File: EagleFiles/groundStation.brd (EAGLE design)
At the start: 100 x 80 mm, 5 parts

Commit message: small changes in motor control
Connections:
- removed net N$13: U$2.GND
- removed net N$14: U$2.FLT_N
- removed net N$26: U$4.FLT_N
- net GND: now also U$2.GND
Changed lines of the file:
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@@
 <contactref element="U$1" pad="GND@0"/>
 <contactref element="U$1" pad="GND@1"/>
+<contactref element="U$2" pad="GND"/>
 <wire x1="-25.4" y1="-38.1" x2="-25.4" y2="-48.26" width="0" layer="19" extent="1-1"/>
 <wire x1="-2.54" y1="-48.26" x2="-25.4" y2="-48.26" width="0" layer="19" extent="1-1"/>
@@
 <wire x1="15.24" y1="-46.99" x2="-2.54" y2="-48.26" width="0" layer="19" extent="1-1"/>
 <wire x1="15.24" y1="-31.75" x2="15.24" y2="-46.99" width="0" layer="19" extent="1-1"/>
-<wire x1="15.24" y1="-6.35" x2="15.24" y2="-31.75" width="0" layer="19" extent="1-1"/>
+<wire x1="15.24" y1="-21.59" x2="15.24" y2="-31.75" width="0" layer="19" extent="1-1"/>
+<wire x1="15.24" y1="-6.35" x2="15.24" y2="-21.59" width="0" layer="19" extent="1-1"/>
 </signal>
 <signal name="N$5">
@@
 <wire x1="26.67" y1="-30.48" x2="15.24" y2="-41.91" width="0" layer="19" extent="1-1"/>
 </signal>
-<signal name="N$13">
-<contactref element="U$2" pad="GND"/>
-</signal>
-<signal name="N$14">
-<contactref element="U$2" pad="FLT_N"/>
-</signal>
 <signal name="V_EXTERNAL">
 <contactref element="U$2" pad="VMOT"/>
@@
 <wire x1="15.24" y1="-29.21" x2="15.24" y2="-3.81" width="0" layer="19" extent="1-1"/>
 </signal>
-<signal name="N$26">
-<contactref element="U$4" pad="FLT_N"/>
-</signal>
 <signal name="AD0">

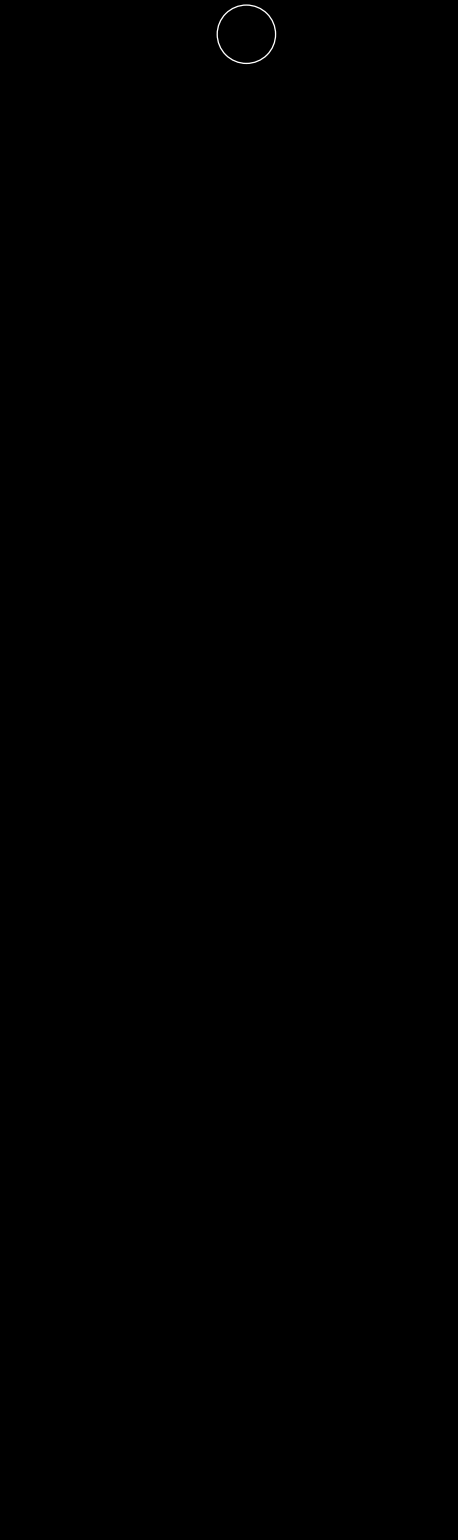
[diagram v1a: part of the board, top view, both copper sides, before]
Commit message: added basic circuit for rffm tp4056
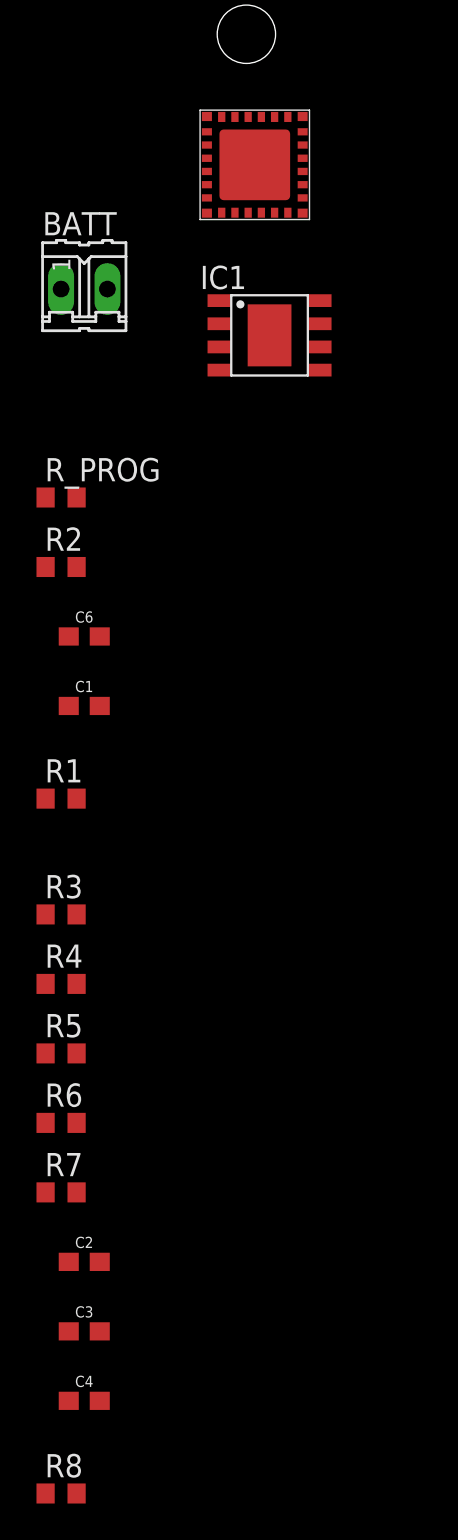
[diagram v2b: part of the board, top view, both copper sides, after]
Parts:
- added BATT: (no value), con-amp-quick:02P
- added C1, C6: 10uf, SparkFun-Capacitors:0603
- added C2: 220nf, SparkFun-Capacitors:0603
- added C3, C4: 1uf, SparkFun-Capacitors:0603
- added IC1: TP4056, TP4056:SOP-8
- added R1: .4ohm, adafruit:R0603
- added R2, R3, R_PROG: (no value), adafruit:R0603
- added R4, R5, R6, R7, R8: 50ohm, adafruit:R0603
- added U$3: RFFM6404, RFFM6406:RFFM6406
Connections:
- new net ANT: R7.1
- new net N$1: BATT.2, C6.2, IC1.5
- new net N$12: R4.2, U$3.13
- new net N$13: R5.2, U$3.20
- new net N$14: R6.2, U$3.18
- new net N$15: U$3.17
- new net N$17: U$3.23
- new net N$18: U$3.24
- new net N$19: U$3.2
- new net N$2: C1.2, IC1.4, IC1.8, R1.1
- new net N$20: U$3.3
- new net N$21: U$3.4
- new net N$3: IC1.2, R_PROG.2
- new net N$4: R3.2, R8.2, U$3.10
- new net N$6: R3.1, R8.1
- new net N$7: R7.2, U$3.7
- new net N$9: C2.2, U$3.5
- new net VCC_BATOUT: R1.2
- new net VCC_TX2: C3.1, C4.1, U$3.26
- net GND: now also BATT.1, C1.1, C2.1, C3.2, C4.2, C6.1, IC1.3, R_PROG.1, U$3.1, U$3.11, U$3.12, U$3.15, U$3.19, U$3.21, U$3.22, U$3.27, U$3.28, U$3.6, U$3.8, U$3.9, U$3.D

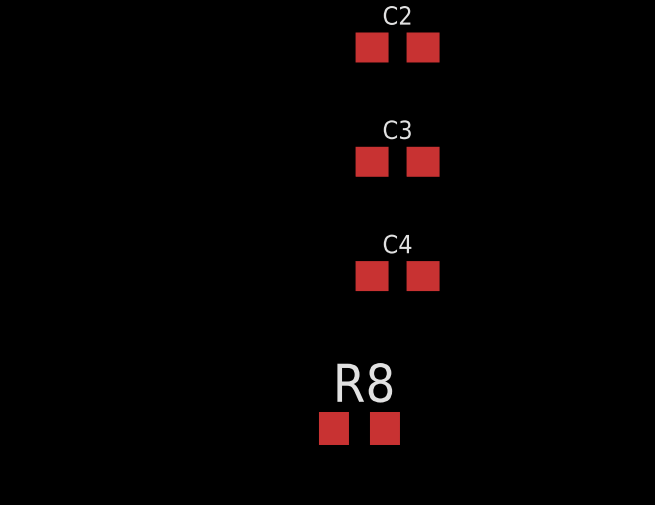
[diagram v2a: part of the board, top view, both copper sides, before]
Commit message: added the basic battery circuit
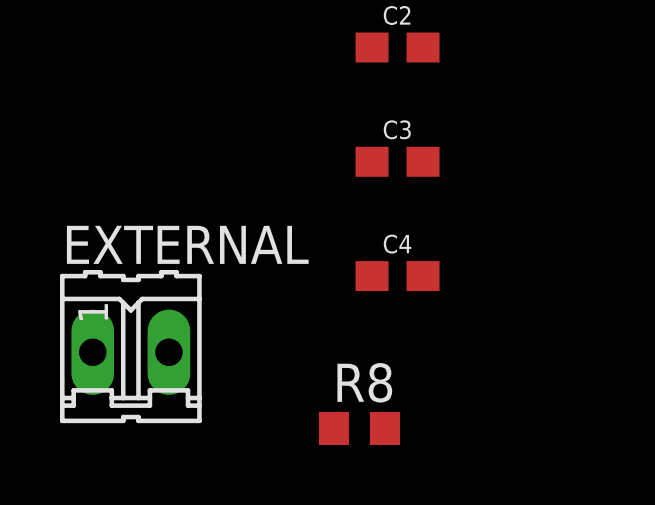
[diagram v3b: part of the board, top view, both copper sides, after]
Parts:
- added EXTERNAL: (no value), con-amp-quick:02P
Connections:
- removed net VCC_BATOUT: R1.2
- removed net VIN: U$1.VIN
- new net RAW_VCC: EXTERNAL.2, R1.2, U$1.VIN
- net GND: now also EXTERNAL.1
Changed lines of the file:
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@@
 <attribute name="VALUE" x="-35.179" y="-136.652" size="1.27" layer="27"/>
+</element>
+<element name="EXTERNAL" library="con-amp-quick" library_urn="urn:adsk.eagle:library:125" package="02P" package3d_urn="urn:adsk.eagle:package:5956/1" value="" x="-41.91" y="-132.08" smashed="yes">
+<attribute name="MF" value="" x="-41.91" y="-132.08" size="1.778" layer="27" display="off"/>
+<attribute name="MPN" value="" x="-41.91" y="-132.08" size="1.778" layer="27" display="off"/>
+<attribute name="NAME" x="-44.196" y="-129.1336" size="1.27" layer="25" ratio="10"/>
+<attribute name="OC_FARNELL" value="unknown" x="-41.91" y="-132.08" size="1.778" layer="27" display="off"/>
+<attribute name="OC_NEWARK" value="unknown" x="-41.91" y="-132.08" size="1.778" layer="27" display="off"/>
+<attribute name="POPULARITY" value="33" x="-41.91" y="-132.08" size="1.778" layer="27" display="off"/>
+<attribute name="VALUE" x="-44.196" y="-135.9154" size="1.27" layer="27" ratio="10"/>
 </element>
 </elements>
@@
 <contactref element="C4" pad="2"/>
 <contactref element="C2" pad="1"/>
+<contactref element="EXTERNAL" pad="1"/>
+<wire x1="-32.17" y1="-129.54" x2="-43.18" y2="-132.08" width="0" layer="19" extent="1-1"/>
 <wire x1="-32.17" y1="-125.73" x2="-32.17" y2="-129.54" width="0" layer="19" extent="1-1"/>
 <wire x1="-33.87" y1="-121.92" x2="-32.17" y2="-125.73" width="0" layer="19" extent="1-1"/>
@@
 <contactref element="U$1" pad="RST"/>
 </signal>
-<signal name="VIN">
-<contactref element="U$1" pad="VIN"/>
-</signal>
 <signal name="STEP2">
 <contactref element="U$1" pad="D2"/>
@@
 <wire x1="-20.11" y1="-69.215" x2="-25.61" y2="-73.025" width="0" layer="19" extent="1-1"/>
 </signal>
-<signal name="VCC_BATOUT">
+<signal name="RAW_VCC">
 <contactref element="R1" pad="2"/>
+<contactref element="EXTERNAL" pad="2"/>
+<contactref element="U$1" pad="VIN"/>
+<wire x1="-33.44" y1="-96.52" x2="-40.64" y2="-132.08" width="0" layer="19" extent="1-1"/>
+<wire x1="-25.4" y1="-50.8" x2="-33.44" y2="-96.52" width="0" layer="19" extent="1-1"/>
 </signal>
 <signal name="N$4">

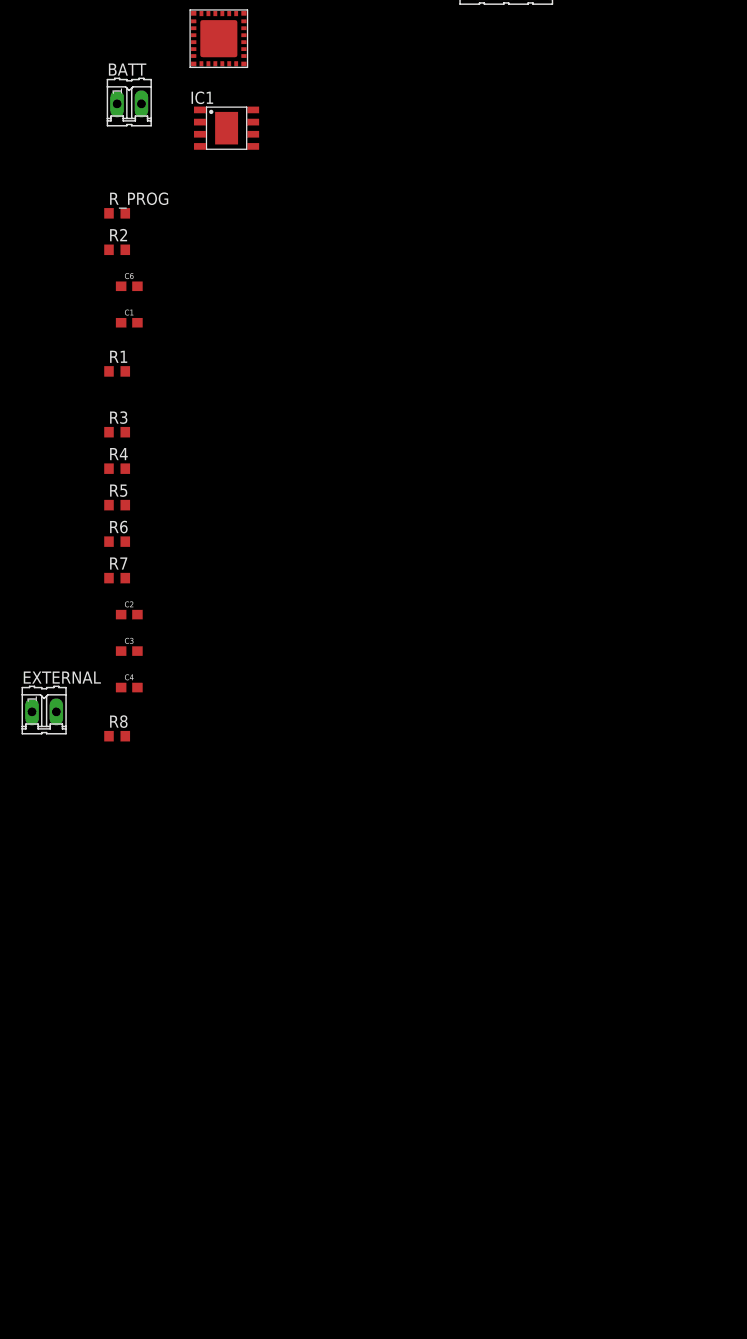
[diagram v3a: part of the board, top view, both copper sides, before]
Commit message: added uass ground station
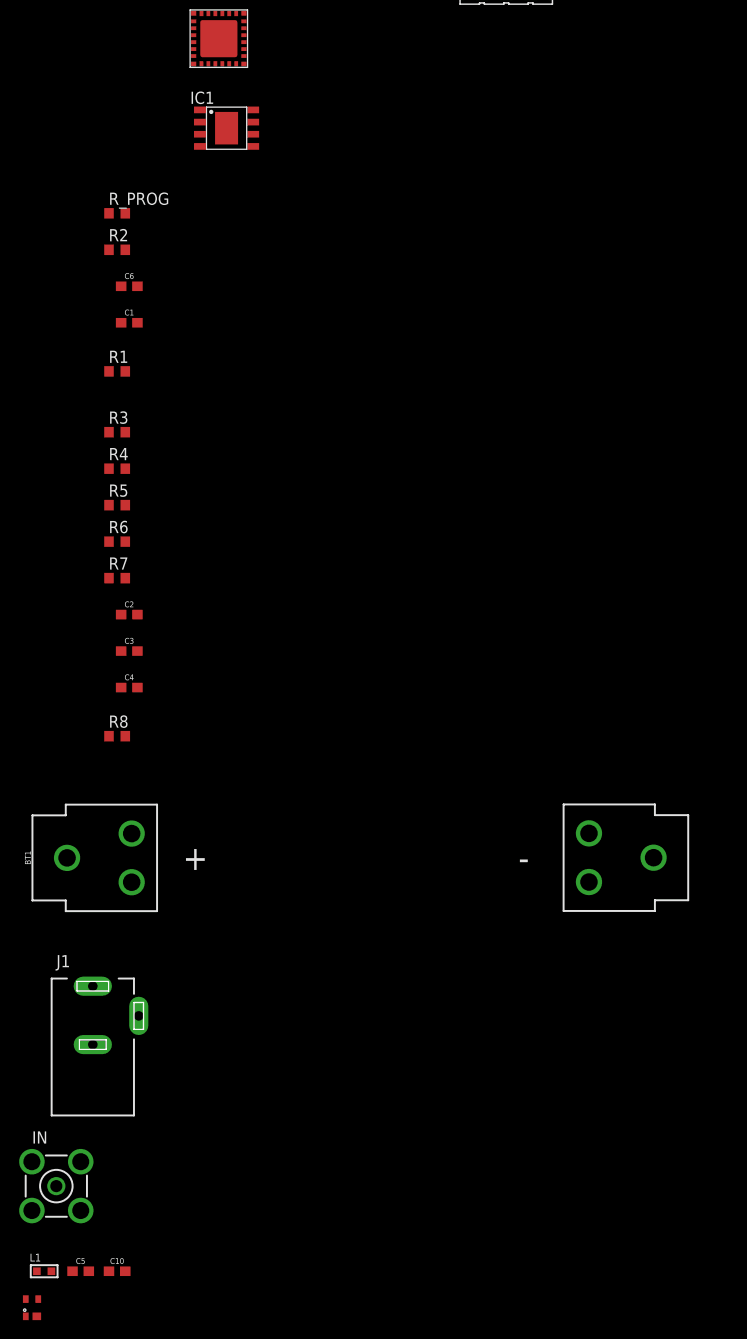
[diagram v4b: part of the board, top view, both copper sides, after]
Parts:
- removed BATT, EXTERNAL: (no value), con-amp-quick:02P
- added BT1: (no value), SparkFun-Batteries:BATTERY_18650-HOLDER
- added C10, C5: 4.7pF, SparkFun-Capacitors:0603
- added IN: BU-SMA-V, con-coax:BU-SMA-V
- added J1: DCJ0202, con-jack:DCJ0202
- added L1: 10uH, rc-master-smd:L0603
- added U$5: PSA4-5043+, PSA4-5043_:PSA4-5043+
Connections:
- new net GND3: IN.2, IN.3, IN.4, IN.5, U$5.2, U$5.4
- new net N$23: C5.2
- new net N$24: C10.1, IN.1
- new net N$25: C10.2, U$5.3
- new net N$26: C5.1, L1.2, U$5.1
- net GND: now also BT1.GND@1, J1.3; no longer BATT.1, EXTERNAL.1
- net N$1: now also BT1.PWR@1; no longer BATT.2
- net RAW_VCC: now also J1.1, L1.1; no longer EXTERNAL.2
